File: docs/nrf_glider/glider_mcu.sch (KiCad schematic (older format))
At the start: 7 parts, among them J1 PROG, J2 Conn_01x12_Male, U1 MSP430G2553IPW20, U2 25LC640, U3 NRF24L01_Breakout

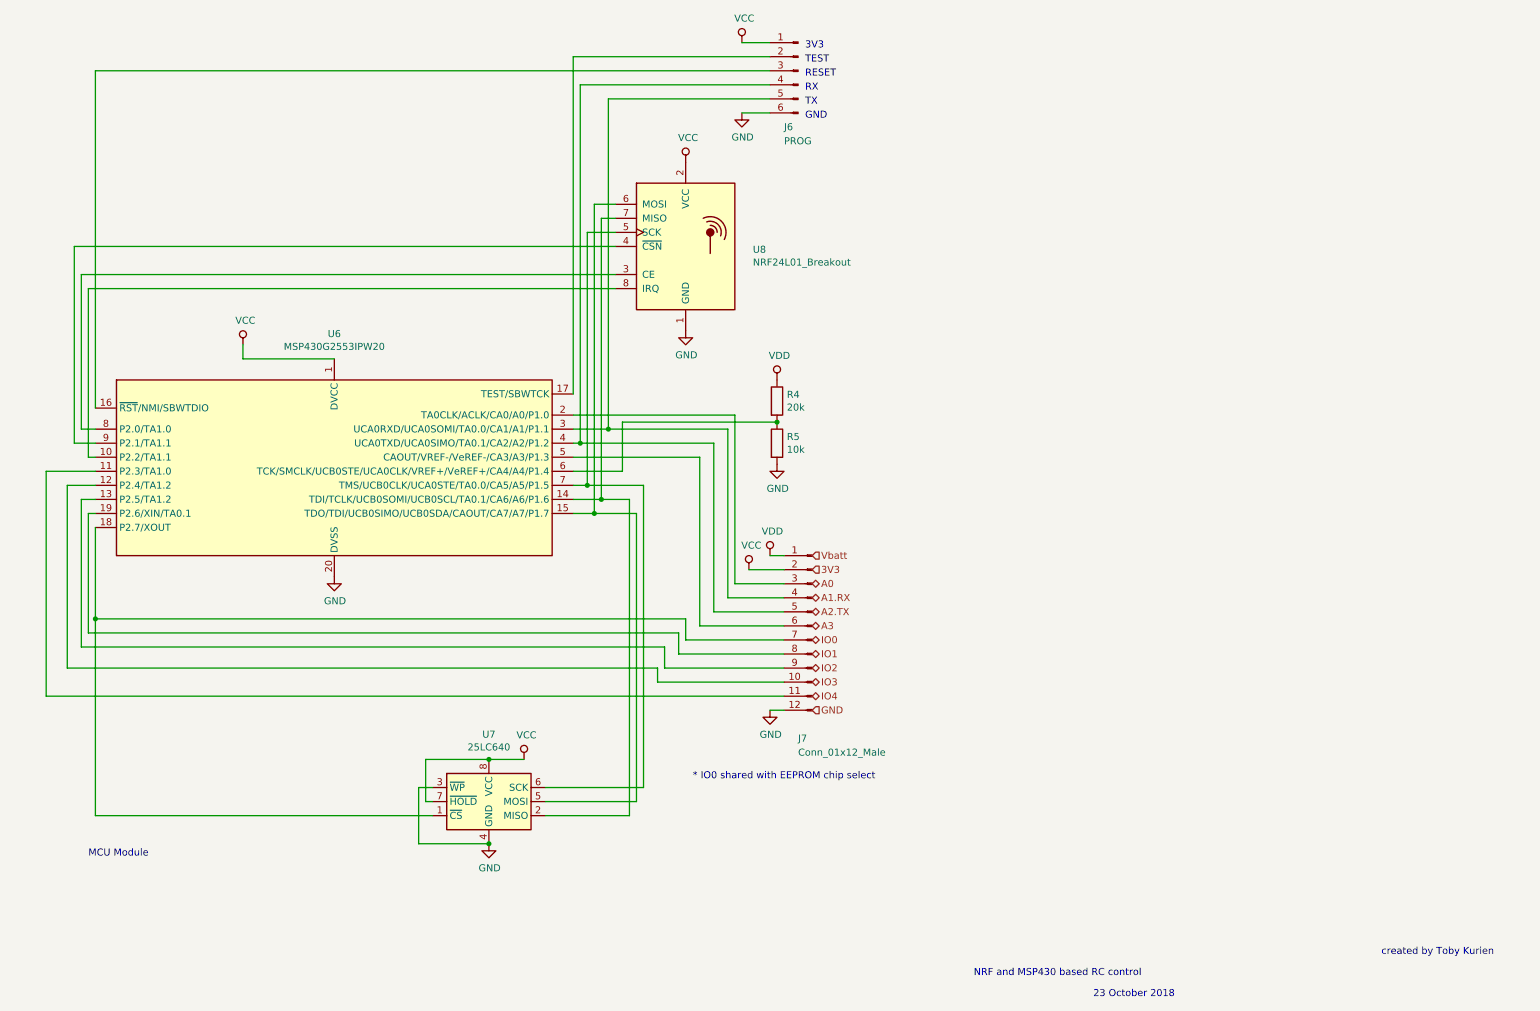
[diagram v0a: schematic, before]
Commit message: Modified pinout to connectors
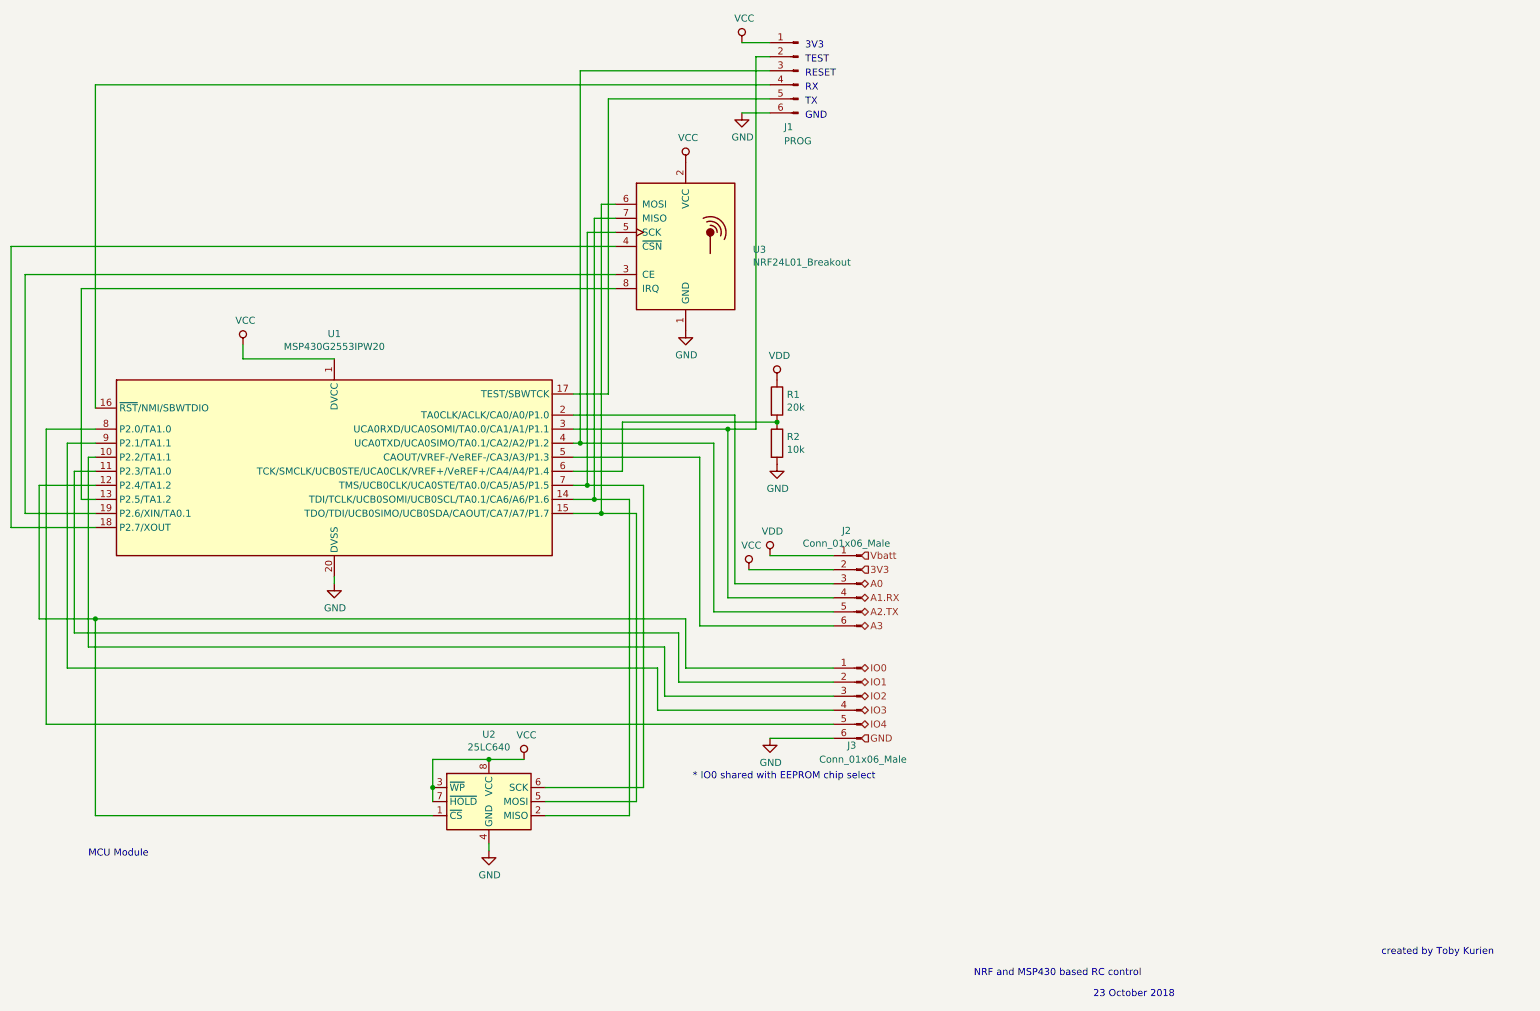
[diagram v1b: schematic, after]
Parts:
- removed J2: Conn_01x12_Male, Connector_PinHeader_2.54mm:PinHeader_1x12_P2.54mm_Vertical, symbol Connector:Conn_01x12_Male
- added J2, J3: Conn_01x06_Male, Connector_PinHeader_2.54mm:PinHeader_1x06_P2.54mm_Vertical, symbol Connector:Conn_01x06_Male
- R1: footprint Resistor_THT:R_Axial_DIN0411_L9.9mm_D3.6mm_P12.70mm_Horizontal -> Resistor_THT:R_Axial_DIN0411_L9.9mm_D3.6mm_P20.32mm_Horizontal
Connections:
- net GND: now also J3.6 (Pin_6); no longer U2.3 (~WP)
- net VCC: now also U2.3 (~WP), J2.2 (Pin_2)
- net VDD: now also J2.1 (Pin_1)
- net at U3.3 (CE): now also U1.19 (P2.6/XIN/TA0.1); no longer U1.8 (P2.0/TA1.0)
- net at U3.4 (~CSN): now also U1.18 (P2.7/XOUT); no longer U1.9 (P2.1/TA1.1)
- net at U3.8 (IRQ): now also U1.13 (P2.5/TA1.2); no longer U1.10 (P2.2/TA1.1)
- net at U1.11 (P2.3/TA1.0): now also J3.2 (Pin_2)
- net at U1.12 (P2.4/TA1.2): now also U2.1 (~CS), J3.1 (Pin_1)
- net at U1.16 (~RST~/NMI/SBWTDIO): now also J1.4 (Pin_4); no longer J1.3 (Pin_3)
- net at U1.17 (TEST/SBWTCK): now also J1.5 (Pin_5); no longer J1.2 (Pin_2)
- net at U1.2 (TA0CLK/ACLK/CA0/A0/P1.0): now also J2.3 (Pin_3)
- net at U1.3 (UCA0RXD/UCA0SOMI/TA0.0/CA1/A1/P1.1): now also J1.2 (Pin_2), J2.4 (Pin_4); no longer J1.5 (Pin_5)
- net at U1.4 (UCA0TXD/UCA0SIMO/TA0.1/CA2/A2/P1.2): now also J1.3 (Pin_3), J2.5 (Pin_5); no longer J1.4 (Pin_4)
- net at U1.5 (CAOUT/VREF-/VeREF-/CA3/A3/P1.3): now also J2.6 (Pin_6)
- new net: J3.3 (Pin_3), U1.10 (P2.2/TA1.1)
- new net: J3.5 (Pin_5), U1.8 (P2.0/TA1.0)
- new net: J3.4 (Pin_4), U1.9 (P2.1/TA1.1)
